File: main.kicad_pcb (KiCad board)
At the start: 2 copper layers, 45 x 73 mm, 21 parts, among them J1 Conn_01x01, J615 Conn_01x04_Male

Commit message: Updated to v1.1 Moved cutout 1.5 mm down Decreased size of earth connection J1
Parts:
- moved BP5 49.2 mm to (124.0, 110.0)
- moved BP1 49.2 mm to (123.6, 70.9)
- moved BP3 49.2 mm to (122.0, 94.5)
- moved BP4 49.2 mm to (90.0, 98.0)
- moved C603 49.2 mm to (119.0, 81.5)
- moved C604 49.2 mm to (89.0, 81.5)
- moved C605 49.2 mm to (116.5, 77.0)
- moved C606 49.2 mm to (91.5, 77.0)
- moved C607 49.2 mm to (122.0, 98.5)
- moved C608 49.2 mm to (95.5, 109.5)
- moved J1 49.2 mm to (121.0, 117.5)
- moved J615 49.2 mm to (105.0, 100.5)
- moved L601 49.2 mm to (124.0, 77.0)
- moved L602 49.2 mm to (124.0, 84.5)
- moved L603 49.2 mm to (103.0, 84.5)
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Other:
- outline, holes or cut-outs redrawn
- board text added: "1.5 mm"
- board text added: "35 µm"
- board text added: "Copper"
- board text added: "Core"
- board text added: "Manufacturing Instruction: - Material FR-4 - Finished thickness: 1.57 mm ± 0.13 mm - Surface finish: HASL - PCBs need not to be RoHS compliant - Do not edit artwork, e.g. to add logos or order numbers - Clean to meet IPC J-STD-001E, Class 2 after assembly"
- board text added: "Material"
- board text added: "Stackup:"
- board text added: "Thickness"
- board text removed: "Place Mill-Max 0507-0-15-15-31-27-10-0 in the MCU pin holes and Mill Max 9081-0-00-15-00-00-08-0 pins on the Teensy side"

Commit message: Increased GND plane clearance to 0.25 mm
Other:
- board text added: "HP 6632B Frontpanel Binding Post PCB v1.1.1 Design: Patrick Baus Date: 2021-07 https://github.com/PatrickBaus"
- board text removed: "HP 6632B Frontpanel Binding Post PCB v1.10 Design: Patrick Baus Date: 2020-10 https://github.com/PatrickBaus"

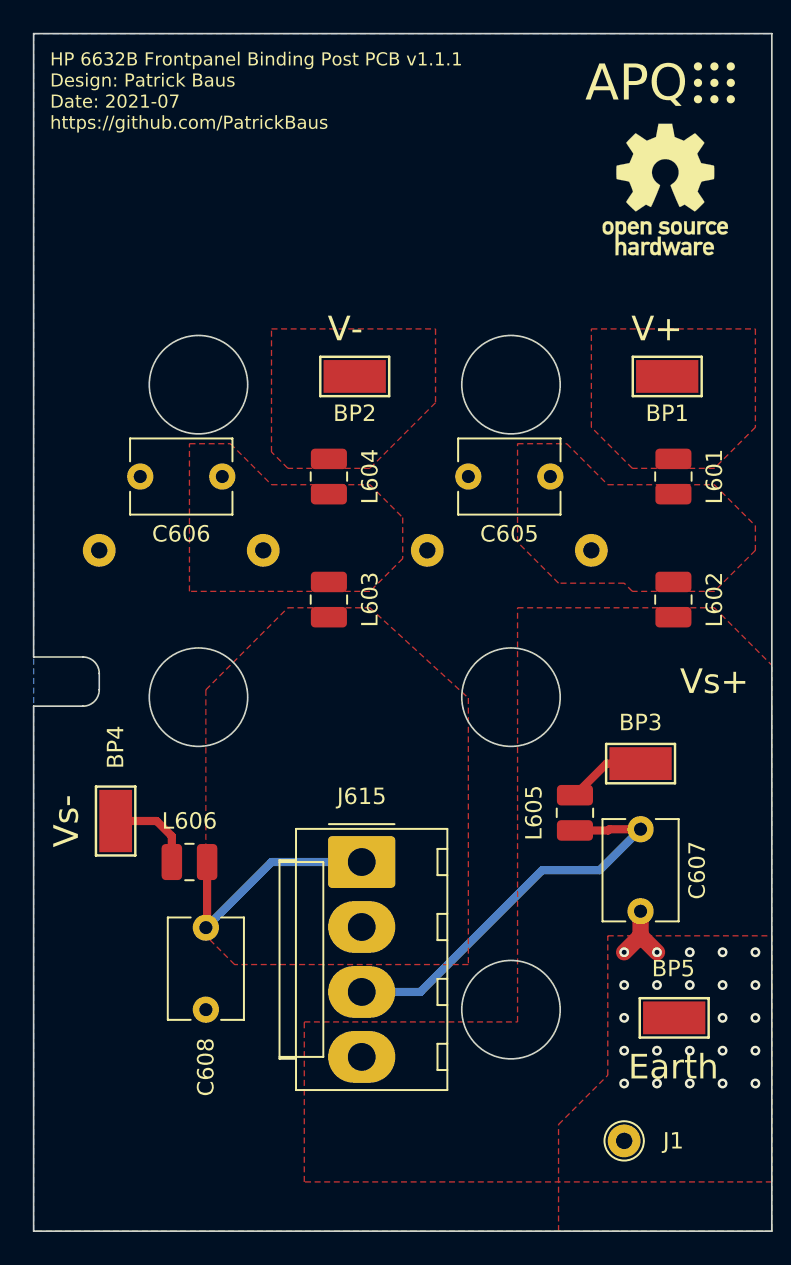
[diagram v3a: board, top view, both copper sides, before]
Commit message: Update to KiCad 8
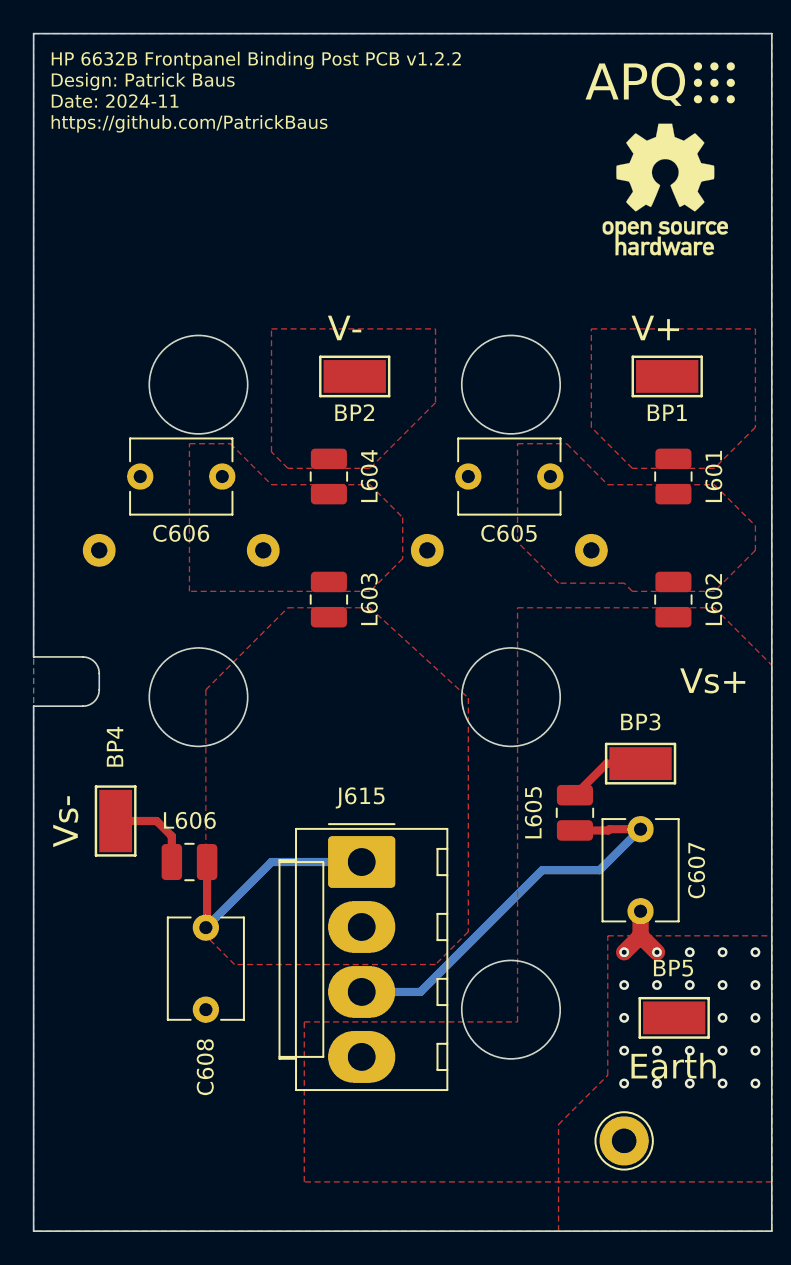
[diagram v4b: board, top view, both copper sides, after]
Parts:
- J1: footprint TestPoint:TestPoint_THTPad_D2.0mm_Drill1.0mm -> TestPoint:TestPoint_THTPad_D3.0mm_Drill1.5mm
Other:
- net class Default removed
- board text added: "HP 6632B Frontpanel Binding Post PCB v1.2.2 Design: Patrick Baus Date: 2024-11 https://github.com/PatrickBaus"
- board text removed: "HP 6632B Frontpanel Binding Post PCB v1.1.1 Design: Patrick Baus Date: 2021-07 https://github.com/PatrickBaus"
